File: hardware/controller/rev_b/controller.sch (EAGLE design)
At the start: 103 parts, among them J1 MODULE_CONTROLLER, J14 SOLDERJUMPERTRACE, J15 SOLDERJUMPERTRACE, J16 SOLDERJUMPERTRACE, J17 SOLDERJUMPERTRACE, J18 MICRO_USB_B_HIROSE_ZX62R-B-5P, J2 DM3AT-SF-PEJM5, J3 U.FL-R-SMT, J5 MICRO_USB_B_HIROSE_ZX62R-B-5P, J6 TC2030-JLINK-L, J7 TC2030-JLINK-L, Q1 DMN32D2LDF, SW1 PTS810SJ, SW2 SIP3240X, SW3 SIP3240X, SW4 SIP3240X, U29 SAM4LC8BA, U3 RXM-GPS-RM-T, U30 SAM4LC8BA, U4 FM25CLXXB-DG, U5 TS3USB30E, U6 FTDI234XD, U7 TXS0108EVQFN20, U8 SN74LVC1G125DBVR, X1 16MHz, X2 16MHz

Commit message: Renumbered parts
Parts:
- removed J17: SOLDERJUMPERTRACE, SparkFun-Passives:SOLDERJUMPERTRACE
- removed J18: MICRO_USB_B_HIROSE_ZX62R-B-5P, connector:MICRO_USB_B_HIROSE_ZX62R-B-5P
- removed U29, U30: SAM4LC8BA, chips:SAM4LC8BA
- added J4: MODULE_CONTROLLER, signpost:MODULE_CONTROLLER
- added J9: SOLDERJUMPERTRACE, SparkFun-Passives:SOLDERJUMPERTRACE
- added U1: FM25CLXXB-DG, chips:FM25CLXXB-DG
- added U2: FTDI234XD, chips:FTDI234XD
- J1: value MODULE_CONTROLLER -> DM3AT-SF-PEJM5; device signpost:MODULE_CONTROLLER -> connector:DM3AT-SF-PEJM5
- J10: value (none) -> SOLDERJUMPERTRACE; device pinhead:PINHD-2X10 -> SparkFun-Passives:SOLDERJUMPERTRACE
- J11, J12: value (none) -> SOLDERJUMPERTRACE; device pinhead:PINHD-1X2 -> SparkFun-Passives:SOLDERJUMPERTRACE
- J14, J15: value SOLDERJUMPERTRACE -> TC2030-JLINK-L; device SparkFun-Passives:SOLDERJUMPERTRACE -> connector:TC2030-JLINK-L
- J16: value SOLDERJUMPERTRACE -> U.FL-R-SMT; device SparkFun-Passives:SOLDERJUMPERTRACE -> connector:U.FL-R-SMT
- J2: value DM3AT-SF-PEJM5 -> MICRO_USB_B_HIROSE_ZX62R-B-5P; device connector:DM3AT-SF-PEJM5 -> connector:MICRO_USB_B_HIROSE_ZX62R-B-5P; DIGIKEY (none) -> H125274CT-ND
- J3: value U.FL-R-SMT -> MICRO_USB_B_HIROSE_ZX62R-B-5P; device connector:U.FL-R-SMT -> connector:MICRO_USB_B_HIROSE_ZX62R-B-5P; DIGIKEY (none) -> H125274CT-ND
- J5: value MICRO_USB_B_HIROSE_ZX62R-B-5P -> (none); device connector:MICRO_USB_B_HIROSE_ZX62R-B-5P -> pinhead:PINHD-1X2; DIGIKEY H125274CT-ND -> (none)
- J6: value TC2030-JLINK-L -> (none); device connector:TC2030-JLINK-L -> pinhead:PINHD-1X2
- J7: value TC2030-JLINK-L -> (none); device connector:TC2030-JLINK-L -> pinhead:PINHD-2X10
- R13: value 100kΩ -> 10kΩ; DIGIKEY 1276-3429-1-ND -> 1276-3431-1-ND
- R17: value 10kΩ -> 100kΩ; DIGIKEY 1276-3431-1-ND -> 1276-3432-1-ND
- R22: DIGIKEY 1276-3432-1-ND -> 1276-3429-1-ND
- R24: value DNP -> 1MΩ; DIGIKEY 1276-3431-1-ND -> 1276-3433-1-ND
- R27: value 1MΩ -> DNP; DIGIKEY 1276-3433-1-ND -> 1276-3431-1-ND
- U4: value FM25CLXXB-DG -> SAM4LC8BA; device chips:FM25CLXXB-DG -> chips:SAM4LC8BA; DIGIKEY FM25CL64B-DGRA-ND -> (none)
- U5: value TS3USB30E -> SAM4LC8BA; device signpost:TS3USB30E -> chips:SAM4LC8BA
- U6: value FTDI234XD -> SN74LVC1G125DBVR; device chips:FTDI234XD -> chips:SN74LVC1G125DBVR
- U7: value TXS0108EVQFN20 -> TS3USB30E; device chips:TXS0108EVQFN20 -> signpost:TS3USB30E; DIGIKEY 296-24806-1-ND -> (none)
- U8: value SN74LVC1G125DBVR -> TXS0108EVQFN20; device chips:SN74LVC1G125DBVR -> chips:TXS0108EVQFN20; DIGIKEY (none) -> 296-24806-1-ND
- renumbered D4 to D1, J472 to J8
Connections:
- net !BACKPLANE_RESET: now also J4G$1.!BACKPLANE_RESET; no longer J1G$1.!BACKPLANE_RESET
- net !CONTROLLER_LED: now also U5.PB11; no longer U30.PB11
- net !CONTROLLER_RESET: now also J15.!RESET, J4CONTROLLER.DBG_!RESET, U5.!RESET; no longer J1CONTROLLER.DBG_!RESET, J7.!RESET, U30.!RESET
- net !EDISON_PWRBTN: now also R16.1, U4.PA05; no longer R17.1, U29.PA05
- net !EDISON_SPI_CS: now also U4.PA22, U8.B4; no longer U29.PA22, U7.B4
- net !EDISON_SPI_CS_1V8: now also J7.13, U8.A4; no longer J10.13, U7.A4
- net !FRAM_CS: now also J7.9, U1.!CS, U5.PA25; no longer J10.9, U30.PA25, U4.!CS
- net !SD_CS: now also J1.DATA3-CD/CS_N, J7.4, R14.1, U4.PA13; no longer J10.4, J2.DATA3-CD/CS_N, R15.1, U29.PA13
- net !SMBALERT: now also J4G$1.!SMBALERT, U5.PA26; no longer J1G$1.!SMBALERT, U30.PA26
- net !STORAGE_CS: now also J7.8, U4.PA09, U5.PB13; no longer J10.8, U29.PA09, U30.PB13
- net !STORAGE_LED: now also U4.PA07; no longer U29.PA07
- net !STORAGE_RESET: now also J14.!RESET, J4STORAGE_MASTER.DBG_!RESET, U4.!RESET; no longer J1STORAGE_MASTER.DBG_!RESET, J6.!RESET, U29.!RESET
- net CONTROLLER_BUCK/LDO_N: now also R27.2, U5.PA02; no longer R24.2, U30.PA02
- net CONTROLLER_DEBUG_GPIO1: now also J4CONTROLLER.DBG_GPIO1, U5.PB14; no longer J1CONTROLLER.DBG_GPIO1, U30.PB14
- net CONTROLLER_DEBUG_GPIO2: now also J4CONTROLLER.DBG_GPIO2, U5.PB15; no longer J1CONTROLLER.DBG_GPIO2, U30.PB15
- net CONTROLLER_DEBUG_RX: now also J4CONTROLLER.DBG_RX, U5.PB04; no longer J1CONTROLLER.DBG_RX, U30.PB04
- net CONTROLLER_DEBUG_TX: now also J4CONTROLLER.DBG_TX, U5.PB05; no longer J1CONTROLLER.DBG_TX, U30.PB05
- net CONTROLLER_SWDCLK: now also J15.SWDCLK, J4CONTROLLER.DBG_SWDCLK, R20.1, U5.TCK; no longer J1CONTROLLER.DBG_SWDCLK, J7.SWDCLK, R21.1, U30.TCK
- net CONTROLLER_SWDIO: now also J15.SWDIO, J4CONTROLLER.DBG_SWDIO, R19.1, U5.PA03; no longer J1CONTROLLER.DBG_SWDIO, J7.SWDIO, R20.1, U30.PA03
- net CONTROLLER_XIN: now also U5.PA00; no longer U30.PA00
- net CONTROLLER_XOUT: now also U5.PA01; no longer U30.PA01
- net D+: now also J2.D+; no longer J18.D+
- net D-: now also J2.D-; no longer J18.D-
- net EDISON_LED1: now also U8.A7; no longer U7.A7
- net EDISON_LED2: now also U8.A8; no longer U7.A8
- net EDISON_SPI_MISO: now also U4.PA20, U8.B3; no longer U29.PA20, U7.B3
- net EDISON_SPI_MISO_1V8: now also J7.12, U8.A3; no longer J10.12, U7.A3
- net EDISON_SPI_MOSI: now also U4.PA19, U8.B2; no longer U29.PA19, U7.B2
- net EDISON_SPI_MOSI_1V8: now also J7.11, U8.A2; no longer J10.11, U7.A2
- net EDISON_SPI_SCLK: now also U4.PA18, U8.B1; no longer U29.PA18, U7.B1
- net EDISON_SPI_SCLK_1V8: now also J7.10, U8.A1; no longer J10.10, U7.A1
- net GND: now also J1.B, J1.GND, J14.GND, J15.GND, J16.P$2, J3.GND, J4CONTROLLER.GND1, J4G$1.GND, J4STORAGE_MASTER.GND1, J5.1, J5.2, J6.1, J6.2, J7.19, R22.2, R27.1, U1.VSS, U2.GND, U4.GND, U4.GNDANA, U5.GNDANA, U6.A, U7.!OE; no longer J10.19, J11.1, J11.2, J12.1, J12.2, J18.GND, J1CONTROLLER.GND1, J1G$1.GND, J1STORAGE_MASTER.GND1, J2.B, J3.P$2, J5.GND, J6.GND, J7.GND, R13.2, R24.1, U29.GND, U29.GNDANA, U30.GND, U30.GNDANA, U4.VSS, U5.!OE, U8.A
- net GPS_ENABLE_POWER: now also R25.1, U5.PB07; no longer R26.1, U30.PB07
- net GPS_IN_RX: now also J7.15, U5.PA20; no longer J10.15, U30.PA20
- net GPS_OUT_TX: now also J7.16, U5.PA19; no longer J10.16, U30.PA19
- net LINUX_5V_IN: now also J10.2; no longer J14.2
- net LINUX_ENABLE_POWER: now also R24.1, U4.PA06; no longer R25.1, U29.PA06
- net MEMORY_MISO: now also J7.7, U1.SO, U4.PA12, U5.PA11; no longer J10.7, U29.PA12, U30.PA11, U4.SO
- net MEMORY_MOSI: now also J7.5, U1.SI, U4.PA11, U5.PA12; no longer J10.5, U29.PA11, U30.PA12, U4.SI
- net MEMORY_SCLK: now also J7.6, U1.SCK, U4.PA10, U5.PA10; no longer J10.6, U29.PA10, U30.PA10, U4.SCK
- net MOD0_IN: now also J4G$1.MOD0_IN, U5.PA04; no longer J1G$1.MOD0_IN, U30.PA04
- net MOD0_OUT: now also J4G$1.MOD0_OUT, U5.PA13; no longer J1G$1.MOD0_OUT, U30.PA13
- net MOD1_IN: now also J4G$1.MOD1_IN, U5.PA05; no longer J1G$1.MOD1_IN, U30.PA05
- net MOD1_OUT: now also J4G$1.MOD1_OUT, U5.PA14; no longer J1G$1.MOD1_OUT, U30.PA14
- net MOD2_IN: now also J4G$1.MOD2_IN, U5.PA06; no longer J1G$1.MOD2_IN, U30.PA06
- net MOD2_OUT: now also J4G$1.MOD2_OUT, U5.PA15; no longer J1G$1.MOD2_OUT, U30.PA15
- net MOD5_IN: now also J4G$1.MOD5_IN, U5.PA07; no longer J1G$1.MOD5_IN, U30.PA07
- net MOD5_OUT: now also J4G$1.MOD5_OUT, U5.PA16; no longer J1G$1.MOD5_OUT, U30.PA16
- net MOD6_IN: now also J4G$1.MOD6_IN, U5.PA08; no longer J1G$1.MOD6_IN, U30.PA08
- net MOD6_OUT: now also J4G$1.MOD6_OUT, U5.PA17; no longer J1G$1.MOD6_OUT, U30.PA17
- net MOD7_IN: now also J4G$1.MOD7_IN, U5.PA09; no longer J1G$1.MOD7_IN, U30.PA09
- net MOD7_OUT: now also J4G$1.MOD7_OUT, U5.PA18; no longer J1G$1.MOD7_OUT, U30.PA18
- net MODULES_SCL: now also J4G$1.MODULES_SCL, U4.PA24, U5.PA24, U8.B6; no longer J1G$1.MODULES_SCL, U29.PA24, U30.PA24, U7.B6
- net MODULES_SCL_1V8: now also U8.A6; no longer U7.A6
- net MODULES_SDA: now also J4G$1.MODULES_SDA, U4.PA23, U5.PA23, U8.B5; no longer J1G$1.MODULES_SDA, U29.PA23, U30.PA23, U7.B5
- net MODULES_SDA_1V8: now also U8.A5; no longer U7.A5
- net N$10: now also J2.+5V; no longer J18.+5V
- net N$12: now also U8.B8; no longer U7.B8
- net N$15: now also J9.2; no longer J15.2
- net N$16: now also J10.1; no longer J14.1
- net N$17: now also U6.Y; no longer U8.Y
- net N$18: now also J12.1; no longer J17.1
- net N$19: now also J11.1; no longer J16.1
- net N$2: now also U2.USBDM; no longer U6.USBDM
- net N$24: now also U2.TXD; no longer U6.TXD
- net N$25: now also U2.RXD; no longer U6.RXD
- net N$28: now also U2.VCC; no longer U6.VCC
- net N$29: now also U4.VDDANA; no longer U29.VDDANA
- net N$3: now also J16.ANT; no longer J3.ANT
- net N$30: now also U7.S; no longer U5.S
- net N$32: now also U5.VDDANA; no longer U30.VDDANA
- net N$34: now also D2.R; no longer D3.R
- net N$37: now also D2.G; no longer D3.G
- net N$38: now also D2.B; no longer D3.B
- net N$4: now also U2.USBDP; no longer U6.USBDP
- net N$44: now also U5.VDDOUT; no longer U30.VDDOUT
- net N$45: now also U4.VDDOUT; no longer U29.VDDOUT
- net N$46: now also U4.VDDCORE; no longer U29.VDDCORE
- net N$48: now also U4.CAPH, U4.CAPL; no longer U29.CAPH, U29.CAPL
- net N$5: now also J3.D-, U7.D1-; no longer J5.D-, U5.D1-
- net N$50: now also U8.B7; no longer U7.B7
- net N$51: now also U4.BIASH, U4.BIASL; no longer U29.BIASH, U29.BIASL
- net N$53: now also U5.BIASH, U5.BIASL; no longer U30.BIASH, U30.BIASL
- net N$54: now also U5.CAPH, U5.CAPL; no longer U30.CAPH, U30.CAPL
- net N$56: now also J11.2; no longer J16.2
- net N$58: now also J1.VCC, J12.2, R13.2, R21.2; no longer J17.2, J2.VCC, R16.2, R22.2
- net N$59: now also U5.VDDCORE; no longer U30.VDDCORE
- net N$6: now also J3.D+, U7.D1+; no longer J5.D+, U5.D1+
- net N$7: now also D3.R; no longer D2.R
- net N$8: now also D3.G; no longer D2.G
- net N$9: now also D3.B; no longer D2.B
- net PPS: now also J4G$1.PPS; no longer J1G$1.PPS
- net SD_DETECT: now also J1.A, R21.1, U4.PA17; no longer J2.A, R22.1, U29.PA17
- net SD_ENABLE_POWER: now also R26.1, U4.PA21; no longer R27.1, U29.PA21
- net SD_MISO: now also J1.DATA0/MISO, J7.2, R15.1, U4.PA15; no longer J10.2, J2.DATA0/MISO, R16.1, U29.PA15
- net SD_MOSI: now also J1.CMD/MOSI, J7.1, R13.1, U4.PA16; no longer J10.1, J2.CMD/MOSI, R14.1, U29.PA16
- net SD_SCLK: now also J1.CLK, J7.3, U4.PA14; no longer J10.3, J2.CLK, U29.PA14
- net SMBCLK: now also J4G$1.SMBCLK, U5.PA22; no longer J1G$1.SMBCLK, U30.PA22
- net SMBDATA: now also J4G$1.SMBDATA, U5.PA21; no longer J1G$1.SMBDATA, U30.PA21
- net STORAGE_BUCK/LDO_N: now also U4.PA02; no longer U29.PA02
- net STORAGE_DEBUG_GPIO1: now also J4STORAGE_MASTER.DBG_GPIO1, U4.PB04; no longer J1STORAGE_MASTER.DBG_GPIO1, U29.PB04
- net STORAGE_DEBUG_GPIO2: now also J4STORAGE_MASTER.DBG_GPIO2, U4.PB05; no longer J1STORAGE_MASTER.DBG_GPIO2, U29.PB05
- net STORAGE_DEBUG_RX: now also J4STORAGE_MASTER.DBG_RX, U4.PB09; no longer J1STORAGE_MASTER.DBG_RX, U29.PB09
- net STORAGE_DEBUG_TX: now also J4STORAGE_MASTER.DBG_TX, U4.PB10; no longer J1STORAGE_MASTER.DBG_TX, U29.PB10
- net STORAGE_SWDCLK: now also J14.SWDCLK, J4STORAGE_MASTER.DBG_SWDCLK, R18.1, U4.TCK; no longer J1STORAGE_MASTER.DBG_SWDCLK, J6.SWDCLK, R19.1, U29.TCK
- net STORAGE_SWDIO: now also J14.SWDIO, J4STORAGE_MASTER.DBG_SWDIO, R17.1, U4.PA03; no longer J1STORAGE_MASTER.DBG_SWDIO, J6.SWDIO, R18.1, U29.PA03
- net STORAGE_XIN: now also U4.PA00; no longer U29.PA00
- net STORAGE_XOUT: now also U4.PA01; no longer U29.PA01
- net USB_D+: now also U7.D+; no longer U5.D+
- net USB_D-: now also U7.D-; no longer U5.D-
- net USB_MOD_D+: now also J4G$1.USB_D+, U7.D2+; no longer J1G$1.USB_D+, U5.D2+
- net USB_MOD_D-: now also J4G$1.USB_D-, U7.D2-; no longer J1G$1.USB_D-, U5.D2-
- net USB_VBUS: now also J3.+5V, R22.1, U6.!OE; no longer J5.+5V, R13.1, U8.!OE
- net VCC_CONTROLLER: now also D3.VDD, J14.VCC, J15.VCC, J4G$1.VCC_CONTROLLER, J7.20, R17.2, R25.2, U1.!HOLD, U1.!WP, U1.VDD, U4.VDDIN, U4.VDDIO, U4.VLCD, U4.VLCDIN, U5.VDDIN, U5.VDDIO, U5.VLCD, U5.VLCDIN; no longer D2.VDD, J10.20, J1G$1.VCC_CONTROLLER, J6.VCC, J7.VCC, R21.2, R27.2, U29.VDDIN, U29.VDDIO, U29.VLCD, U29.VLCDIN, U30.VDDIN, U30.VDDIO, U30.VLCD, U30.VLCDIN, U4.!HOLD, U4.!WP, U4.VDD
- net VCC_LINUX: now also J4G$1.VCC_LINUX, J7.17, J9.1, R24.2, U6.VCC; no longer J10.17, J15.1, J1G$1.VCC_LINUX, R25.2, U8.VCC
- net VCC_LINUX_1V8: now also J7.14, U2.VCCIO, U8.OE, U8.VCCA; no longer J10.14, U6.VCCIO, U7.OE, U7.VCCA
- net VCC_LINUX_3V3: now also D2.VDD, J7.18, R16.2, U7.VCC, U8.VCCB; no longer D3.VDD, J10.18, R17.2, U5.VCC, U7.VCCB

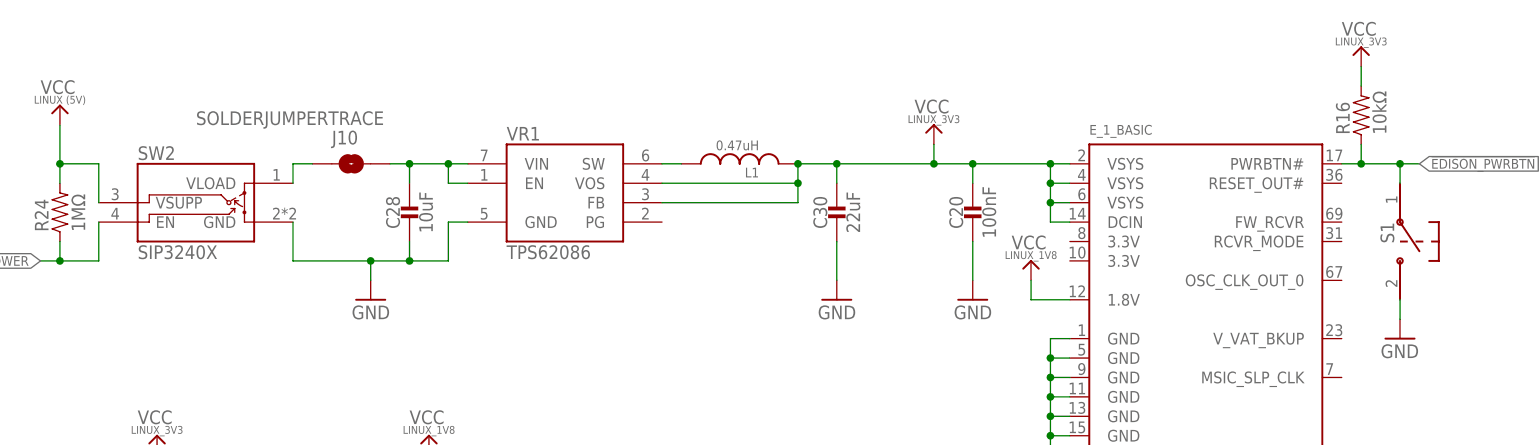
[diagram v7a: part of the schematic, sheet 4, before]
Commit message: Labels placed betterer
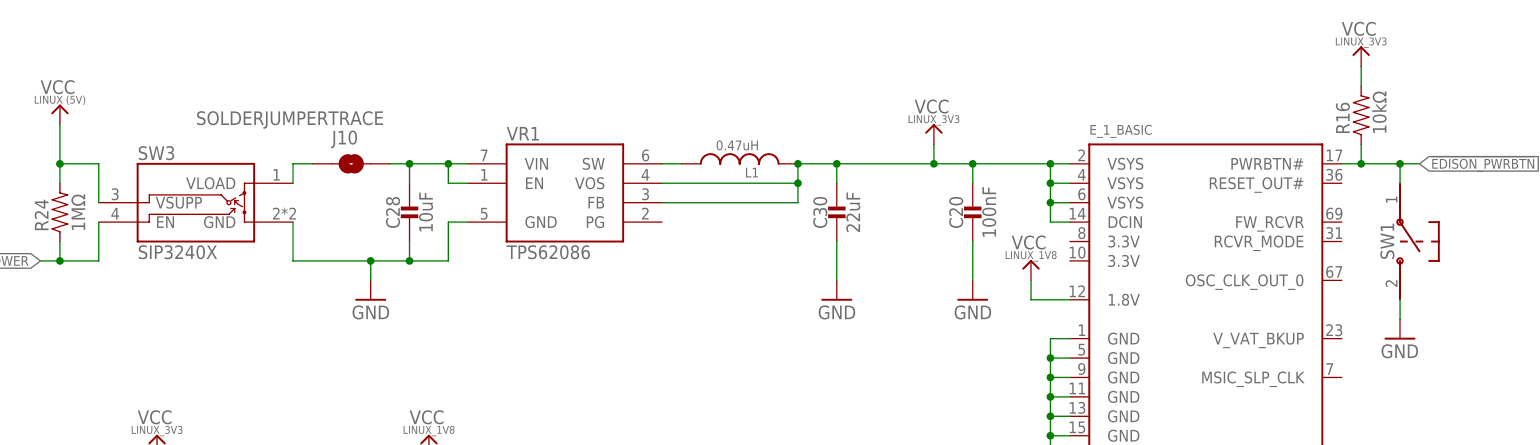
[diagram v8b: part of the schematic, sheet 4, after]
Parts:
- removed S1: B3U-1000P, switches:B3U-1000P
- added SW5: SIP3240X, signpost:SIP3240X
- L1: DIGIKEY (none) -> 490-10596-1-ND
- SW1: value PTS810SJ -> B3U-1000P; device switches:PTS810SJ -> switches:B3U-1000P
- SW2: value SIP3240X -> PTS810SJ; device signpost:SIP3240X -> switches:PTS810SJ
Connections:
- net !BACKPLANE_RESET: now also SW2.P$1; no longer SW1.P$1
- net !EDISON_PWRBTN: now also SW1.P$1; no longer S1.P$1
- net GND: now also SW2.P$2, SW5.GND; no longer S1.P$2, SW2.GND
- net GPS_ENABLE_POWER: now also SW4.EN; no longer SW3.EN
- net LINUX_ENABLE_POWER: now also SW3.EN; no longer SW2.EN
- net N$16: now also SW3.VLOAD; no longer SW2.VLOAD
- net N$18: now also SW5.VLOAD; no longer SW4.VLOAD
- net N$19: now also SW4.VLOAD; no longer SW3.VLOAD
- net SD_ENABLE_POWER: now also SW5.EN; no longer SW4.EN
- net VCC_CONTROLLER: now also SW5.VSUPP; no longer SW3.VSUPP
- net VCC_LINUX: now also SW3.VSUPP; no longer SW2.VSUPP
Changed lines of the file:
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@@
 </part>
 <part name="U$6" library="signpost" deviceset="VCC_LINUX" device=""/>
-<part name="SW2" library="signpost" deviceset="SIP3240X" device=""/>
+<part name="SW3" library="signpost" deviceset="SIP3240X" device=""/>
 <part name="R24" library="passives" deviceset="RESISTOR" device="0402_RES" value="1MΩ">
 <attribute name="DIGIKEY" value="1276-3433-1-ND"/>
@@
 <part name="GND15" library="umich" deviceset="GND" device=""/>
 <part name="L1" library="passives" deviceset="INDUCTOR" device="DFE322512C" value="0.47uH">
+<attribute name="DIGIKEY" value="490-10596-1-ND"/>
 <attribute name="MOUSER" value="81-1277AS-H-R47MP2"/>
 </part>
@@
 <part name="J7" library="pinhead" deviceset="PINHD-2X10" device=""/>
 <part name="LOGO1" library="logos" deviceset="UMICH_SOLID" device="_MEDIUM" value="UMICH_SOLID_MEDIUM"/>
-<part name="SW1" library="switches" deviceset="PTS810SJ" device=""/>
+<part name="SW2" library="switches" deviceset="PTS810SJ" device=""/>
 <part name="J5" library="pinhead" deviceset="PINHD-1X2" device=""/>
 <part name="J6" library="pinhead" deviceset="PINHD-1X2" device=""/>
@@
 </part>
 <part name="U$27" library="signpost" deviceset="VCC_LINUX_3V3" device=""/>
-<part name="SW3" library="signpost" deviceset="SIP3240X" device=""/>
+<part name="SW4" library="signpost" deviceset="SIP3240X" device=""/>
 <part name="R25" library="passives" deviceset="RESISTOR" device="0402_RES" value="1MΩ">
 <attribute name="DIGIKEY" value="1276-3433-1-ND"/>
@@
 <part name="J11" library="SparkFun-Passives" deviceset="SOLDERJUMPER" device="TRACE"/>
 <part name="U$28" library="signpost" deviceset="VCC_CONTROLLER" device=""/>
-<part name="SW4" library="signpost" deviceset="SIP3240X" device=""/>
+<part name="SW5" library="signpost" deviceset="SIP3240X" device=""/>
 <part name="R26" library="passives" deviceset="RESISTOR" device="0402_RES" value="1MΩ">
 <attribute name="DIGIKEY" value="1276-3433-1-ND"/>
@@
 </part>
 <part name="GND38" library="umich" deviceset="GND" device=""/>
-<part name="S1" library="switches" deviceset="B3U" device="-1000P"/>
+<part name="SW1" library="switches" deviceset="B3U" device="-1000P"/>
 <part name="GND39" library="umich" deviceset="GND" device=""/>
 <part name="D1" library="passives" deviceset="DIODE" device="">
@@
 <instance part="J7" gate="A" x="45.72" y="53.34"/>
 <instance part="LOGO1" gate="G$1" x="231.14" y="22.86"/>
-<instance part="SW1" gate="G$1" x="203.2" y="53.34"/>
+<instance part="SW2" gate="G$1" x="203.2" y="53.34"/>
 <instance part="J5" gate="G$1" x="48.26" y="27.94"/>
 <instance part="J6" gate="G$1" x="48.26" y="15.24"/>
@@
 <wire x1="210.82" y1="53.34" x2="213.36" y2="53.34" width="0.1524" layer="91"/>
 <wire x1="213.36" y1="53.34" x2="213.36" y2="50.8" width="0.1524" layer="91"/>
-<pinref part="SW1" gate="G$1" pin="P$2"/>
+<pinref part="SW2" gate="G$1" pin="P$2"/>
 </segment>
 <segment>
@@
 <wire x1="193.04" y1="53.34" x2="195.58" y2="53.34" width="0.1524" layer="91"/>
 <label x="193.04" y="53.34" size="1.27" layer="95" rot="R180" xref="yes"/>
-<pinref part="SW1" gate="G$1" pin="P$1"/>
+<pinref part="SW2" gate="G$1" pin="P$1"/>
 </segment>
 </net>
@@
 <attribute name="DIGIKEY" x="233.68" y="86.36" size="1.27" layer="96" align="bottom-center" display="off"/>
 </instance>
-<instance part="SW3" gate="G$1" x="144.78" y="40.64"/>
+<instance part="SW4" gate="G$1" x="144.78" y="40.64"/>
 <instance part="R25" gate="G$1" x="127" y="43.18" rot="R90">
 <attribute name="DIGIKEY" x="127" y="43.18" size="1.27" layer="96" font="vector" rot="R90" display="off"/>
@@
 <wire x1="172.72" y1="40.64" x2="172.72" y2="33.02" width="0.1524" layer="91"/>
 <junction x="172.72" y="33.02"/>
-<pinref part="SW3" gate="G$1" pin="GND"/>
+<pinref part="SW4" gate="G$1" pin="GND"/>
 <wire x1="157.48" y1="40.64" x2="157.48" y2="33.02" width="0.1524" layer="91"/>
 <wire x1="157.48" y1="33.02" x2="167.64" y2="33.02" width="0.1524" layer="91"/>
@@
 <pinref part="R25" gate="G$1" pin="2"/>
 <wire x1="127" y1="45.72" x2="127" y2="48.26" width="0.1524" layer="91"/>
-<pinref part="SW3" gate="G$1" pin="VSUPP"/>
+<pinref part="SW4" gate="G$1" pin="VSUPP"/>
 <wire x1="132.08" y1="43.18" x2="132.08" y2="48.26" width="0.1524" layer="91"/>
 <wire x1="132.08" y1="48.26" x2="127" y2="48.26" width="0.1524" layer="91"/>
@@
 <wire x1="127" y1="35.56" x2="124.46" y2="35.56" width="0.1524" layer="91"/>
 <label x="124.46" y="35.56" size="1.27" layer="95" font="vector" rot="R180" xref="yes"/>
-<pinref part="SW3" gate="G$1" pin="EN"/>
+<pinref part="SW4" gate="G$1" pin="EN"/>
 <wire x1="132.08" y1="40.64" x2="132.08" y2="35.56" width="0.1524" layer="91"/>
 <wire x1="132.08" y1="35.56" x2="127" y2="35.56" width="0.1524" layer="91"/>
@@
 <net name="N$19" class="0">
 <segment>
-<pinref part="SW3" gate="G$1" pin="VLOAD"/>
+<pinref part="SW4" gate="G$1" pin="VLOAD"/>
 <wire x1="157.48" y1="50.8" x2="157.48" y2="45.72" width="0.1524" layer="91"/>
 <pinref part="J11" gate="1" pin="1"/>
@@
 <instance part="GND28" gate="1" x="195.58" y="81.28" rot="MR0"/>
 <instance part="U$23" gate="G$1" x="172.72" y="104.14"/>
-<instance part="SW4" gate="G$1" x="139.7" y="48.26"/>
+<instance part="SW5" gate="G$1" x="139.7" y="48.26"/>
 <instance part="R26" gate="G$1" x="121.92" y="50.8" rot="R90">
 <attribute name="DIGIKEY" x="121.92" y="50.8" size="1.27" layer="96" font="vector" rot="R90" display="off"/>
@@
 <wire x1="157.48" y1="58.42" x2="157.48" y2="33.02" width="0.1524" layer="91"/>
 <junction x="157.48" y="33.02"/>
-<pinref part="SW4" gate="G$1" pin="GND"/>
+<pinref part="SW5" gate="G$1" pin="GND"/>
 <wire x1="152.4" y1="48.26" x2="152.4" y2="33.02" width="0.1524" layer="91"/>
 <junction x="152.4" y="33.02"/>
@@
 <pinref part="R26" gate="G$1" pin="2"/>
 <wire x1="121.92" y1="53.34" x2="121.92" y2="55.88" width="0.1524" layer="91"/>
-<pinref part="SW4" gate="G$1" pin="VSUPP"/>
+<pinref part="SW5" gate="G$1" pin="VSUPP"/>
 <wire x1="127" y1="50.8" x2="127" y2="55.88" width="0.1524" layer="91"/>
 <wire x1="127" y1="55.88" x2="121.92" y2="55.88" width="0.1524" layer="91"/>
@@
 <wire x1="121.92" y1="43.18" x2="119.38" y2="43.18" width="0.1524" layer="91"/>
 <label x="119.38" y="43.18" size="1.27" layer="95" font="vector" rot="R180" xref="yes"/>
-<pinref part="SW4" gate="G$1" pin="EN"/>
+<pinref part="SW5" gate="G$1" pin="EN"/>
 <wire x1="127" y1="48.26" x2="127" y2="43.18" width="0.1524" layer="91"/>
 <wire x1="127" y1="43.18" x2="121.92" y2="43.18" width="0.1524" layer="91"/>
@@
 <net name="N$18" class="0">
 <segment>
-<pinref part="SW4" gate="G$1" pin="VLOAD"/>
+<pinref part="SW5" gate="G$1" pin="VLOAD"/>
 <pinref part="J12" gate="1" pin="1"/>
 <wire x1="152.4" y1="53.34" x2="152.4" y2="55.88" width="0.1524" layer="91"/>
@@
 <instance part="U$2" gate="G$1" x="45.72" y="154.94"/>
 <instance part="U$3" gate="G$1" x="160.02" y="152.4"/>
-<instance part="SW2" gate="G$1" x="63.5" y="142.24"/>
+<instance part="SW3" gate="G$1" x="63.5" y="142.24"/>
 <instance part="R24" gate="G$1" x="45.72" y="144.78" rot="R90">
 <attribute name="DIGIKEY" x="45.72" y="144.78" size="1.27" layer="96" font="vector" rot="R90" display="off"/>
@@
 <instance part="L1" gate="G$1" x="134.62" y="149.86" rot="R90">
 <attribute name="MOUSER" x="134.62" y="149.86" size="1.27" layer="96" font="vector" rot="R90" display="off"/>
+<attribute name="DIGIKEY" x="134.62" y="149.86" size="1.778" layer="96" rot="R90" display="off"/>
 </instance>
 <instance part="C28" gate="G$1" x="91.44" y="144.78">
@@
 </instance>
 <instance part="U$27" gate="G$1" x="215.9" y="162.56"/>
-<instance part="S1" gate="G$1" x="220.98" y="139.7" rot="R270"/>
+<instance part="SW1" gate="G$1" x="220.98" y="139.7" rot="R270"/>
 <instance part="GND39" gate="1" x="220.98" y="127"/>
 </instances>
@@
 <wire x1="91.44" y1="139.7" x2="91.44" y2="137.16" width="0.1524" layer="91"/>
 <junction x="91.44" y="137.16"/>
-<pinref part="SW2" gate="G$1" pin="GND"/>
+<pinref part="SW3" gate="G$1" pin="GND"/>
 <wire x1="76.2" y1="142.24" x2="76.2" y2="137.16" width="0.1524" layer="91"/>
 <wire x1="76.2" y1="137.16" x2="86.36" y2="137.16" width="0.1524" layer="91"/>
@@
 </segment>
 <segment>
-<pinref part="S1" gate="G$1" pin="P$2"/>
+<pinref part="SW1" gate="G$1" pin="P$2"/>
 <pinref part="GND39" gate="1" pin="GND"/>
 <wire x1="220.98" y1="129.54" x2="220.98" y2="132.08" width="0.1524" layer="91"/>
@@
 <wire x1="45.72" y1="137.16" x2="43.18" y2="137.16" width="0.1524" layer="91"/>
 <label x="43.18" y="137.16" size="1.27" layer="95" font="vector" rot="R180" xref="yes"/>
-<pinref part="SW2" gate="G$1" pin="EN"/>
+<pinref part="SW3" gate="G$1" pin="EN"/>
 <wire x1="50.8" y1="142.24" x2="50.8" y2="137.16" width="0.1524" layer="91"/>
 <wire x1="50.8" y1="137.16" x2="45.72" y2="137.16" width="0.1524" layer="91"/>
@@
 <pinref part="R24" gate="G$1" pin="2"/>
 <wire x1="45.72" y1="147.32" x2="45.72" y2="149.86" width="0.1524" layer="91"/>
-<pinref part="SW2" gate="G$1" pin="VSUPP"/>
+<pinref part="SW3" gate="G$1" pin="VSUPP"/>
 <wire x1="50.8" y1="144.78" x2="50.8" y2="149.86" width="0.1524" layer="91"/>
 <wire x1="50.8" y1="149.86" x2="45.72" y2="149.86" width="0.1524" layer="91"/>
@@
 <wire x1="215.9" y1="149.86" x2="215.9" y2="152.4" width="0.1524" layer="91"/>
 <junction x="215.9" y="149.86"/>
-<pinref part="S1" gate="G$1" pin="P$1"/>
+<pinref part="SW1" gate="G$1" pin="P$1"/>
 <wire x1="220.98" y1="147.32" x2="220.98" y2="149.86" width="0.1524" layer="91"/>
 <junction x="220.98" y="149.86"/>
@@
 <net name="N$16" class="0">
 <segment>
-<pinref part="SW2" gate="G$1" pin="VLOAD"/>
+<pinref part="SW3" gate="G$1" pin="VLOAD"/>
 <wire x1="76.2" y1="147.32" x2="76.2" y2="149.86" width="0.1524" layer="91"/>
 <pinref part="J10" gate="1" pin="1"/>
